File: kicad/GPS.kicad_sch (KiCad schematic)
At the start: 20 parts, among them J1 Conn_01x03_Pin, J2 Conn_01x03_Pin, J3 Conn_01x03_Pin, J4 Conn_01x03_Pin, SW1 SW_SPST, SW2 SW_SPST, U2 ATGM332D-5N31, U3 PE4259

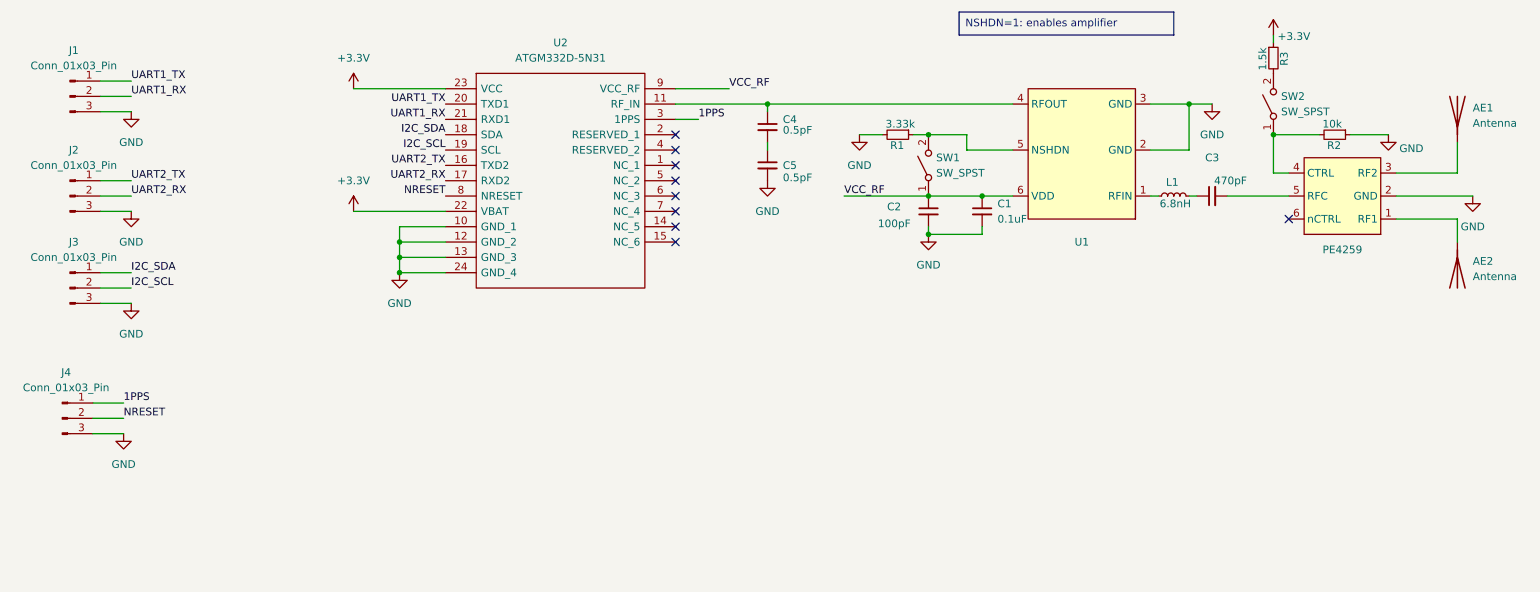
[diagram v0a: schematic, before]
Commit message: fixed issues with footprints and symbols, minor connections drawn | TODO: DC-DC regulator empty footprint
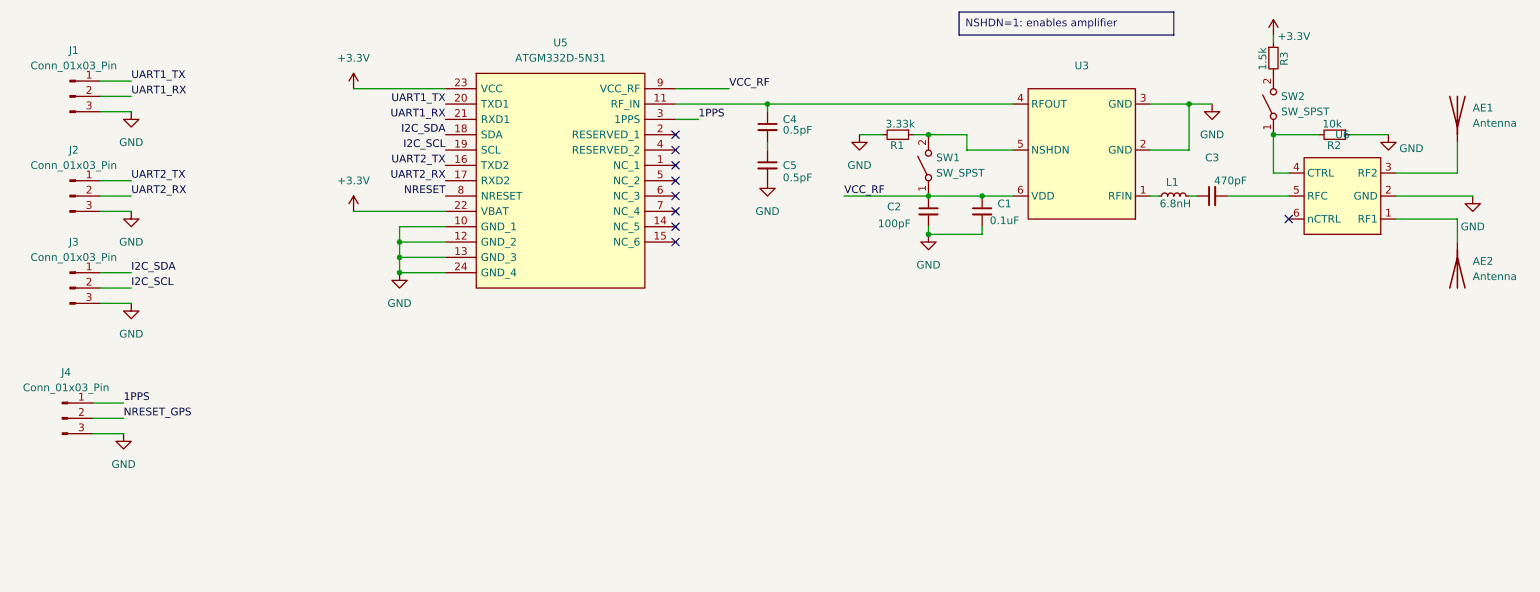
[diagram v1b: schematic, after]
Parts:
- removed U1: ~, Package_TO_SOT_SMD:SOT-23-6, symbol wireless_testboard:AT2659S
- removed U2: ATGM332D-5N31, ATGM332D-5N31:ATGM332D5N31, symbol wireless_testboard:ATGM332D-5N31
- removed U3: PE4259, Package_TO_SOT_SMD:SOT-363_SC-70-6_Handsoldering, symbol wireless_testboard:PE4259
- added U3: ~, Package_TO_SOT_SMD:SOT-23-6_Handsoldering, symbol hw_wireless_testboard:AT2659S
- added U5: ATGM332D-5N31, hw_wireless_testboard:ATGM332D5N31, symbol hw_wireless_testboard:ATGM332D-5N31
- added U6: ~, Package_TO_SOT_SMD:SOT-363_SC-70-6_Handsoldering, symbol hw_wireless_testboard:PE4259
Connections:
- net +3.3V: now also U5.22 (VBAT), U5.23 (VCC)
- net 1PPS: now also U5.3 (1PPS)
- net GND: now also U3.2 (GND), U3.3 (GND), U5.10 (GND_1), U5.12 (GND_2), U5.13 (GND_3), U5.24 (GND_4), U6.2 (GND)
- net I2C_SCL: now also U5.19 (SCL)
- net I2C_SDA: now also U5.18 (SDA)
- net NRESET: now also U5.8 (NRESET); no longer J4.2 (Pin_2)
- net UART1_RX: now also U5.21 (RXD1)
- net UART1_TX: now also U5.20 (TXD1)
- net UART2_RX: now also U5.17 (RXD2)
- net UART2_TX: now also U5.16 (TXD2)
- net VCC_RF: now also U3.6 (VDD), U5.9 (VCC_RF)
- net at R2.2, SW2.1 (A): now also U6.4 (CTRL)
- net at AE2.1 (A): now also U6.1 (RF1)
- net at R1.1, SW1.2 (B): now also U3.5 (NSHDN)
- net at L1.1: now also U3.1 (RFIN)
- net at C4.1: now also U3.4 (RFOUT), U5.11 (RF_IN)
- net at AE1.1 (A): now also U6.3 (RF2)
- net at C3.2: now also U6.5 (RFC)
- new net NRESET_GPS: J4.2 (Pin_2)

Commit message: finished bluetooth schematic apart from anteantenna-design, WiFi design started
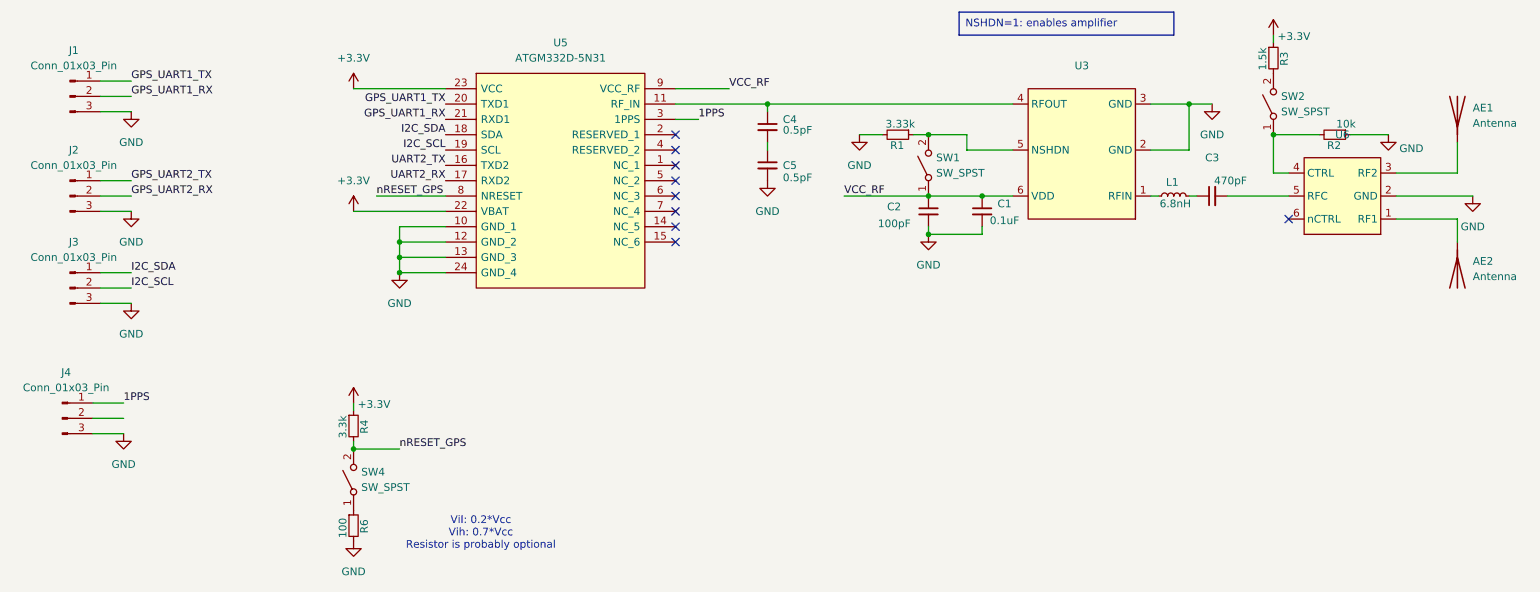
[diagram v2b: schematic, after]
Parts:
- added R4: 3.3k, symbol Device:R_Small
- added R6: 100, symbol Device:R_Small
- added SW4: SW_SPST, symbol Switch:SW_SPST
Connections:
- net +3.3V: now also R4.1
- net GND: now also R6.2
- net UART2_RX: no longer J2.2 (Pin_2)
- net UART2_TX: no longer J2.1 (Pin_1)
- net NRESET renamed nRESET_GPS
- net nRESET_GPS: now also R4.2, SW4.2 (B)
- net NRESET_GPS: no longer names the net of J4.2 (Pin_2)
- net UART1_RX renamed GPS_UART1_RX
- net UART1_TX renamed GPS_UART1_TX
- new net: R6.1, SW4.1 (A)
- new net GPS_UART2_RX: J2.2 (Pin_2)
- new net GPS_UART2_TX: J2.1 (Pin_1)
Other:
- note added: "Vil: 0.2*Vcc Vih: 0.7*Vcc Resistor is probably optional"
